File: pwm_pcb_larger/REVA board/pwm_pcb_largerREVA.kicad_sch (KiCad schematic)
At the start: 84 parts, among them J1 Conn_01x02, J10 Conn_01x02, J11 Conn_01x02, J12 Conn_01x02, J13 Conn_01x02, J14 Conn_01x02, J15 Conn_01x02, J16 Conn_01x02, J17 Conn_01x02, J18 Conn_01x02, J2 Conn_01x02, J3 Conn_01x02, J4 Conn_01x02, J5 Conn_01x02, J6 Conn_01x02, J7 Conn_01x02, J8 Conn_01x02, J9 Conn_01x02, Q1 NMOS, Q10 NMOS, Q11 NMOS, Q12 NMOS, Q13 NMOS, Q14 NMOS, Q15 NMOS, Q16 NMOS, Q17 Q_PMOS_DGS, Q2 NMOS, Q3 NMOS, Q4 NMOS, Q5 NMOS, Q6 NMOS, Q7 NMOS, Q8 NMOS, Q9 NMOS, SW1 SW_SPST, U1 ESP32_DevKit_V1_DOIT, U2 LM317_TO-252

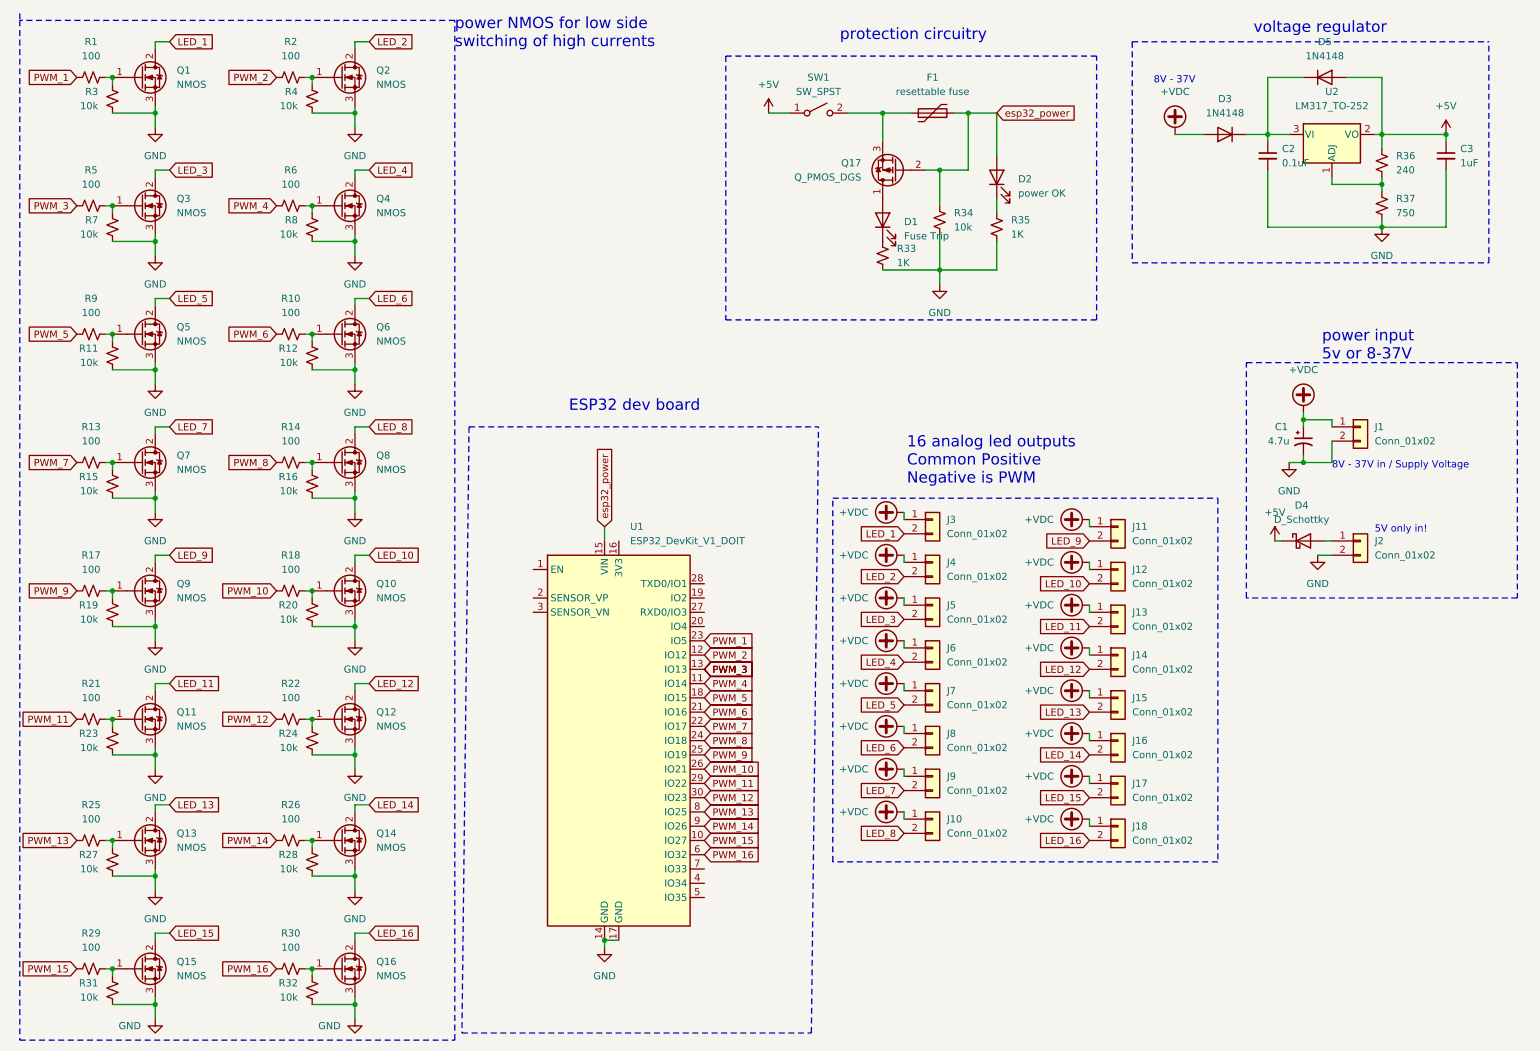
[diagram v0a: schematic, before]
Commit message: starting rev b with new connectors
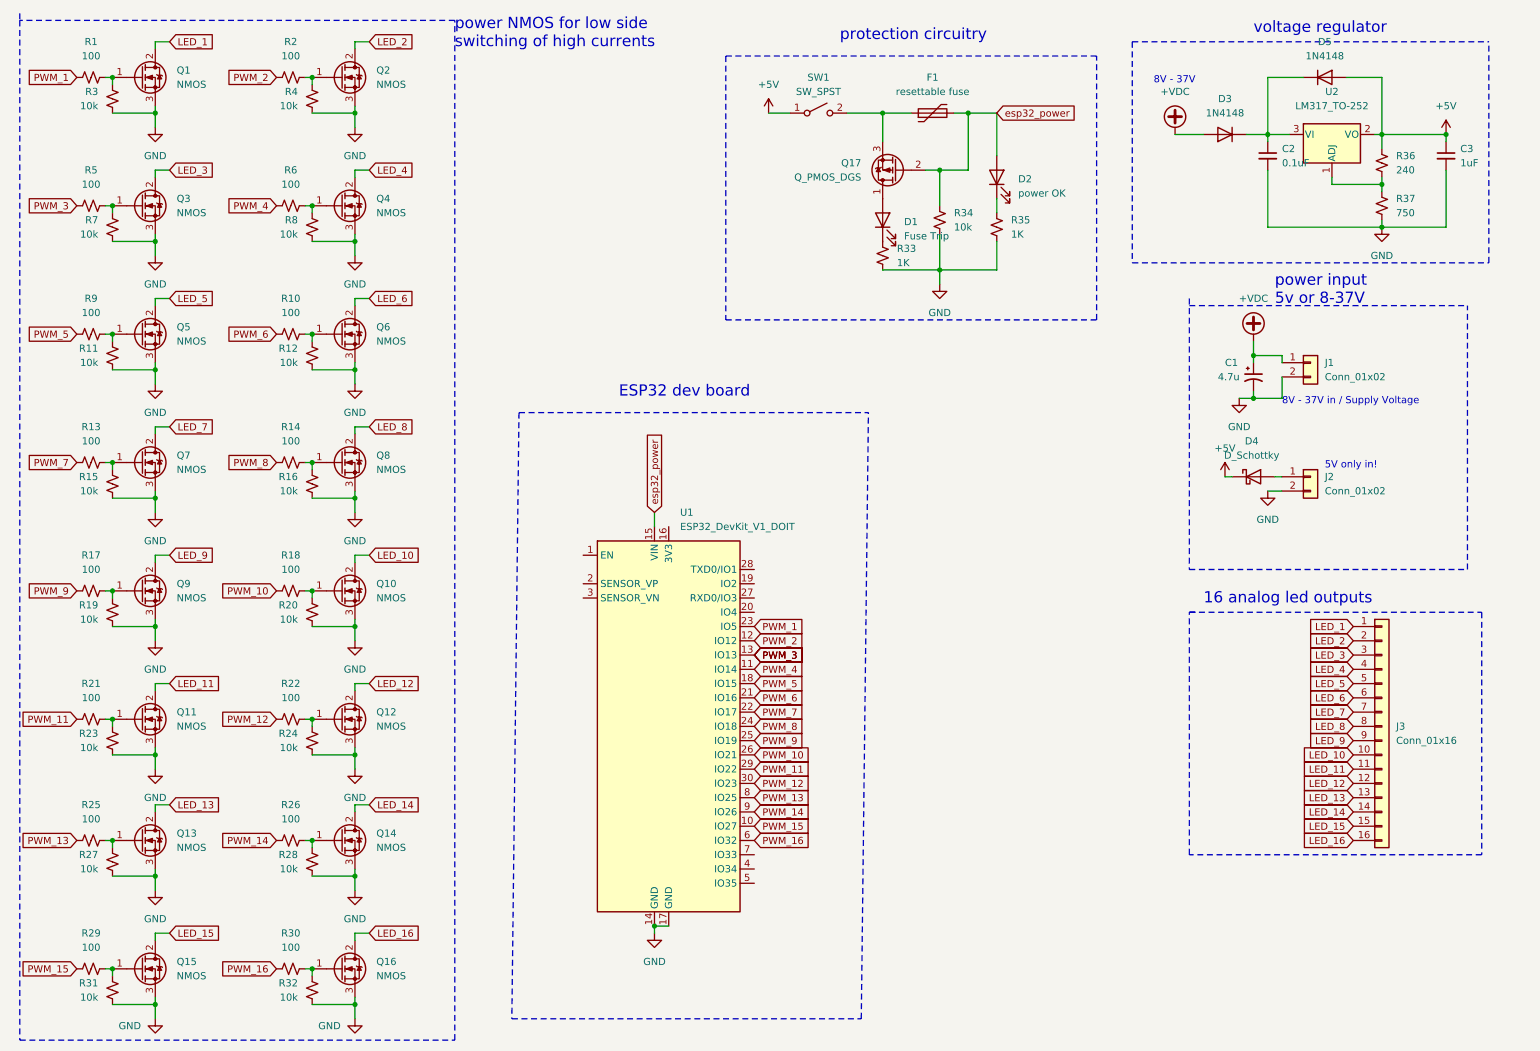
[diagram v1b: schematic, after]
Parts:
- removed J10, J11, J12, J13, J14, J15, J16, J17, J18, J3, J4, J5, J6, J7, J8, J9: Conn_01x02, Connector_Molex:Molex_Micro-Fit_3.0_43650-0200_1x02_P3.00mm_Horizontal, symbol Connector_Generic:Conn_01x02
- added J3: Conn_01x16, william_custom:CUI_TBP02R1-381-16BE, symbol Connector_Generic:Conn_01x16
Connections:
- net LED_1: now also J3.1 (Pin_1)
- net LED_10: now also J3.10 (Pin_10)
- net LED_11: now also J3.11 (Pin_11)
- net LED_12: now also J3.12 (Pin_12)
- net LED_13: now also J3.13 (Pin_13)
- net LED_14: now also J3.14 (Pin_14)
- net LED_15: now also J3.15 (Pin_15)
- net LED_16: now also J3.16 (Pin_16)
- net LED_2: now also J3.2 (Pin_2)
- net LED_3: now also J3.3 (Pin_3)
- net LED_4: now also J3.4 (Pin_4)
- net LED_5: now also J3.5 (Pin_5)
- net LED_6: now also J3.6 (Pin_6)
- net LED_7: now also J3.7 (Pin_7)
- net LED_8: now also J3.8 (Pin_8)
- net LED_9: now also J3.9 (Pin_9)
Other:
- note added: "16 analog led outputs"
- note removed: "16 analog led outputs Common Positive Negative is PWM"
- moved on the sheet: C1, D4, J1, J2, U1
